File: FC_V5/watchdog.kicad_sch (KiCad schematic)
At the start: 40 parts, among them J10 Breakout, J11 Breakout, U1 TLV1704

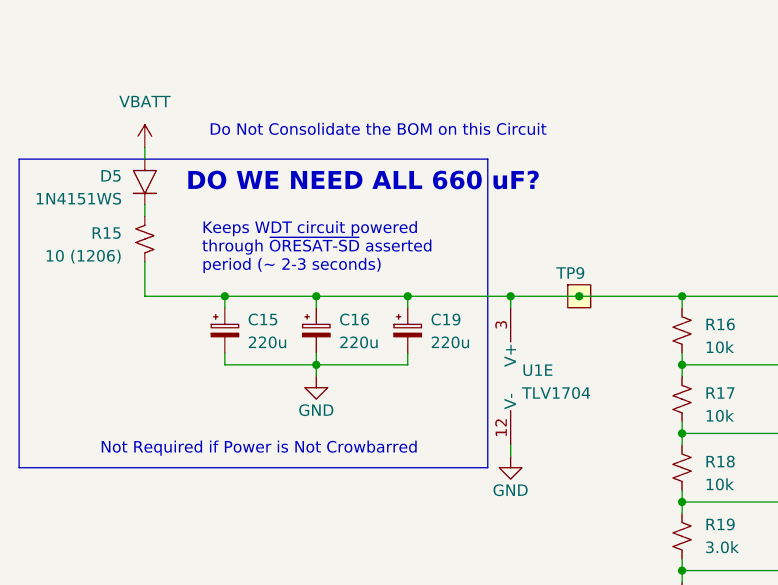
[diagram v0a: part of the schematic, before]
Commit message: Removed Unneed WDT Caps
We didn't need those caps because they are only required for OreSat.

NOTE: ALL OF THE SCHEMATIC REFERENCES ARE BUSTED AHHHHH
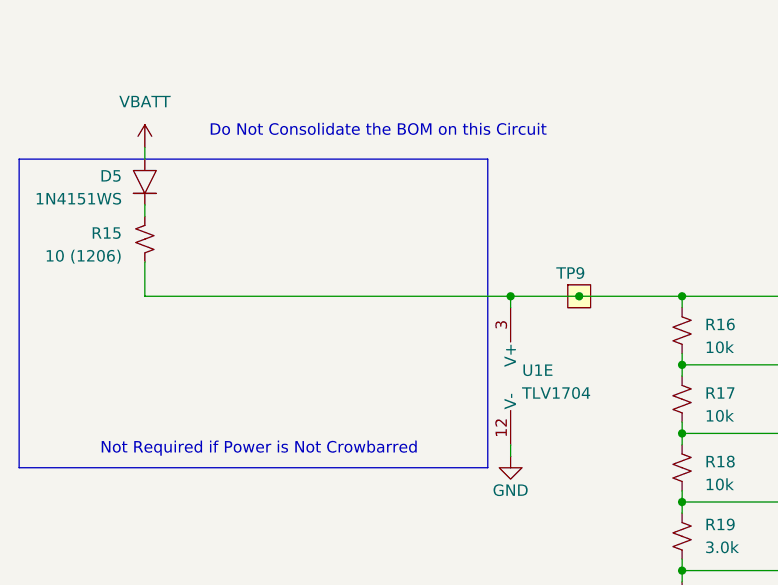
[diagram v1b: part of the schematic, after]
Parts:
- removed C15, C16, C19: 220u, Capacitor_Tantalum_SMD:CP_EIA-7361-38_AVX-V, symbol Device:C_Polarized_Small
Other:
- note removed: "DO WE NEED ALL 660 uF?"
- note removed: "Keeps WDT circuit powered through ~{ORESAT-SD} asserted period (~ 2-3 seconds)"

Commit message: More Stuff!
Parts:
- removed J10: Breakout, Connector_PinHeader_2.54mm:PinHeader_1x04_P2.54mm_Vertical, symbol Connector_Generic:Conn_01x04
- removed J11: Breakout, FC_DEV_BOARD:JST_BM04B-SRSS-TB(LF)(SN), symbol Connector_Generic:Conn_01x04
- removed JP2: SolderJumper_2_Open, Jumper:SolderJumper-2_P1.3mm_Open_RoundedPad1.0x1.5mm, symbol Jumper:SolderJumper_2_Open
- added C26, C28: 100nf, Capacitor_SMD:C_0402_1005Metric, symbol Adafruit ItsyBitsy RP2040-eagle-import:CAP_CERAMIC_0402NO
- added R23: 47k, Resistor_SMD:R_0603_1608Metric, symbol Device:R_Small_US
- added U3: AP22652, SOT26:SOT26, symbol Power_Management:AP22652
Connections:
- net GND: now also C26.2, C28.2, U3.2 (GND)
- net VBATT renamed WDT_BIAS
- net WDT_BIAS: now also C28.1, U3.6 (Output)
- new net: R23.2, U3.5 (ILIM)
- new net +3V3: C26.1, R23.1, U3.1 (Input)
- new net WDT_ENABLE: U3.3 (EN)
- no-connect marks 0 -> 1
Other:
- note removed: "Backup 5V Bias"

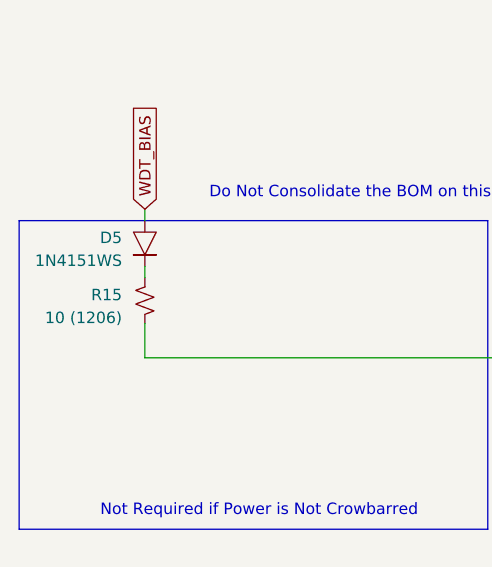
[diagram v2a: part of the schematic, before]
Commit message: Refactored Layout
The additional radio is on the top of the board now!
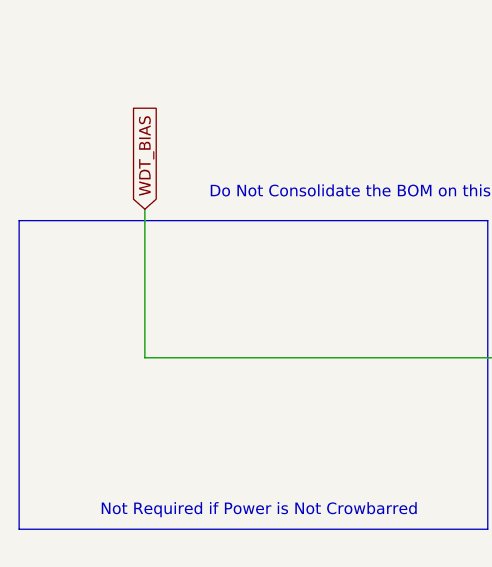
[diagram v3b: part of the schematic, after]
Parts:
- removed D5: 1N4151WS, Diode_SMD:D_SOD-323, symbol oresat-diodes:1N4151WS-HE3
- removed R15: 10 (1206), Resistor_SMD:R_1206_3216Metric, symbol Device:R_Small_US
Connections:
- net WDT-VIN is gone; now on net WDT_BIAS: R16.1, R30.1, R36.2, TP9.1, U1.3 (V+)
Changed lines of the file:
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@@
 	(wire
 		(pts
+			(xy 29.21 44.45) (xy 29.21 60.96)
+		)
+		(stroke
+			(width 0)
+			(type default)
+		)
+	)
+	(wire
+		(pts
 			(xy 88.9 68.58) (xy 185.42 68.58)
 		)
@@
 	(wire
 		(pts
-			(xy 29.21 57.15) (xy 29.21 60.96)
-		)
-		(stroke
-			(width 0)
-			(type default)
-		)
-	)
-	(wire
-		(pts
 			(xy 77.47 60.96) (xy 88.9 60.96)
 		)
@@
 	(wire
 		(pts
-			(xy 29.21 44.45) (xy 29.21 45.72)
-		)
-		(stroke
-			(width 0)
-			(type default)
-		)
-	)
-	(wire
-		(pts
 			(xy 201.93 142.24) (xy 204.47 142.24)
 		)
@@
 	(wire
 		(pts
-			(xy 29.21 50.8) (xy 29.21 52.07)
-		)
-		(stroke
-			(width 0)
-			(type default)
-		)
-	)
-	(wire
-		(pts
 			(xy 125.73 35.56) (xy 129.54 35.56)
 		)
@@
 	)
 	(symbol
-		(lib_id "oresat-diodes:1N4151WS-HE3")
-		(at 29.21 48.26 90)
-		(mirror x)
-		(unit 1)
-		(exclude_from_sim no)
-		(in_bom yes)
-		(on_board yes)
-		(dnp no)
-		(property "Reference" "D5"
-			(at 26.67 47.625 90)
-			(effects
-				(font
-					(size 1.27 1.27)
-				)
-				(justify left)
-			)
-		)
-		(property "Value" "1N4151WS"
-			(at 26.67 50.165 90)
-			(effects
-				(font
-					(size 1.27 1.27)
-				)
-				(justify left)
-			)
-		)
-		(property "Footprint" "Diode_SMD:D_SOD-323"
-			(at 34.29 48.26 0)
-			(effects
-				(font
-					(size 1.27 1.27)
-				)
-				(hide yes)
-			)
-		)
-		(property "Datasheet" "https://www.vishay.com/docs/85847/1n4151ws.pdf"
-			(at 36.83 48.26 0)
-			(effects
-				(font
-					(size 1.27 1.27)
-				)
-				(hide yes)
-			)
-		)
-		(property "Description" "Diode Standard 50V 150mA Surface Mount SOD-323"
-			(at 29.21 48.26 0)
-			(effects
-				(font
-					(size 1.27 1.27)
-				)
-				(hide yes)
-			)
-		)
-		(property "DPN" "112-1N4151WS-E3-08CT-ND"
-			(at 29.21 48.26 0)
-			(effects
-				(font
-					(size 1.27 1.27)
-				)
-				(hide yes)
-			)
-		)
-		(property "DST" "Digi-Key"
-			(at 29.21 48.26 0)
-			(effects
-				(font
-					(size 1.27 1.27)
-				)
-				(hide yes)
-			)
-		)
-		(property "MFR" "Vishay"
-			(at 29.21 48.26 0)
-			(effects
-				(font
-					(size 1.27 1.27)
-				)
-				(hide yes)
-			)
-		)
-		(property "MPN" "1N4151WS-E3-08"
-			(at 29.21 48.26 0)
-			(effects
-				(font
-					(size 1.27 1.27)
-				)
-				(hide yes)
-			)
-		)
-		(pin "1"
-		)
-		(pin "2"
-		)
-		(instances
-			(project "FC_V5"
-				(path "/c64c0d72-a9f6-4f3a-891e-1f647558f538/d3e26510-981a-4dd5-9b7d-a587e6324dc6"
-					(reference "D5")
-					(unit 1)
-				)
-			)
-		)
-	)
-	(symbol
 		(lib_id "Device:C_Small")
 		(at 170.18 128.27 0)
@@
 					(unit 1)
 				)
-			)
-		)
-	)
-	(symbol
-		(lib_id "Device:R_Small_US")
-		(at 29.21 54.61 0)
-		(mirror y)
-		(unit 1)
-		(exclude_from_sim no)
-		(in_bom yes)
-		(on_board yes)
-		(dnp no)
-		(property "Reference" "R15"
-			(at 26.67 53.975 0)
-			(effects
-				(font
-					(size 1.27 1.27)
-				)
-				(justify left)
-			)
-		)
-		(property "Value" "10 (1206)"
-			(at 26.67 56.515 0)
-			(effects
-				(font
-					(size 1.27 1.27)
-				)
-				(justify left)
-			)
-		)
-		(property "Footprint" "Resistor_SMD:R_1206_3216Metric"
-			(at 29.21 54.61 0)
-			(effects
-				(font
-					(size 1.27 1.27)
-				)
-				(hide yes)
-			)
-		)
-		(property "Datasheet" "~"
-			(at 29.21 54.61 0)
-			(effects
-				(font
-					(size 1.27 1.27)
-				)
-				(hide yes)
-			)
-		)
-		(property "Description" "10 Ohms ±1% 0.5W, 1/2W Chip Resistor 1206 (3216 Metric) Automotive AEC-Q200, Pulse Withstanding Thick Film"
-			(at 29.21 54.61 0)
-			(effects
-				(font
-					(size 1.27 1.27)
-				)
-				(hide yes)
-			)
-		)
-		(property "DPN" "RHM10.0AFCT-ND"
-			(at 29.21 54.61 0)
-			(effects
-				(font
-					(size 1.27 1.27)
-				)
-				(hide yes)
-			)
-		)
-		(property "DST" "Digi-Key"
-			(at 29.21 54.61 0)
-			(effects
-				(font
-					(size 1.27 1.27)
-				)
-				(hide yes)
-			)
-		)
-		(property "MFR" "Rohm Semiconductor"
-			(at 29.21 54.61 0)
-			(effects
-				(font
-					(size 1.27 1.27)
-				)
-				(hide yes)
-			)
-		)
-		(property "MPN" "ESR18EZPF10R0"
-			(at 29.21 54.61 0)
-			(effects
-				(font
-					(size 1.27 1.27)
-				)
-				(hide yes)
-			)
-		)
-		(pin "1"
-		)
-		(pin "2"
-		)
-		(instances
-			(project "FC_V5"
-				(path "/c64c0d72-a9f6-4f3a-891e-1f647558f538/d3e26510-981a-4dd5-9b7d-a587e6324dc6"
-					(reference "R15")
-					(unit 1)
-				)

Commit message: Almost Done with Layout!
Just been the VReg reset circuit and the V_RF Regulator and we are ready to rock and roll
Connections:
- net +3V3: now also R37.2
- net WDT_BIAS: no longer R37.2
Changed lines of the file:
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@@
 	(global_label "WDT_BIAS"
 		(shape input)
-		(at 238.76 64.77 90)
-		(fields_autoplaced yes)
-		(effects
-			(font
-				(size 1.27 1.27)
-			)
-			(justify left)
-		)
-		(property "Intersheetrefs" "${INTERSHEET_REFS}"
-			(at 238.76 52.9553 90)
-			(effects
-				(font
-					(size 1.27 1.27)
-				)
-				(justify left)
-				(hide yes)
-			)
-		)
-	)
-	(global_label "WDT_BIAS"
-		(shape input)
 		(at 29.21 44.45 90)
 		(fields_autoplaced yes)
@@
 					(unit 1)
 				)
+			)
+		)
+	)
+	(symbol
+		(lib_id "power:+3V3")
+		(at 238.76 64.77 0)
+		(unit 1)
+		(exclude_from_sim no)
+		(in_bom yes)
+		(on_board yes)
+		(dnp no)
+		(property "Reference" "#PWR0100"
+			(at 238.76 68.58 0)
+			(effects
+				(font
+					(size 1.27 1.27)
+				)
+				(hide yes)
+			)
+		)
+		(property "Value" "+3V3"
+			(at 234.696 63.5 0)
+			(effects
+				(font
+					(size 1.27 1.27)
+				)
+			)
+		)
+		(property "Footprint" ""
+			(at 238.76 64.77 0)
+			(effects
+				(font
+					(size 1.27 1.27)
+				)
+				(hide yes)
+			)
+		)
+		(property "Datasheet" ""
+			(at 238.76 64.77 0)
+			(effects
+				(font
+					(size 1.27 1.27)
+				)
+				(hide yes)
+			)
+		)
+		(property "Description" "Power symbol creates a global label with name \"+3V3\""
+			(at 238.76 64.77 0)
+			(effects
+				(font
+					(size 1.27 1.27)
+				)
+				(hide yes)
+			)
+		)
+		(pin "1"
+		)
+		(instances
+			(project "FC_V5"
+				(path "/c64c0d72-a9f6-4f3a-891e-1f647558f538/d3e26510-981a-4dd5-9b7d-a587e6324dc6"
+					(reference "#PWR0100")
+					(unit 1)
+				)

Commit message: Added a bunch of components
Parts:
- C20, C21, C22, C23, C24: value 10u -> 10uF
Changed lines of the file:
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@@
 			)
 		)
-		(property "Value" "10u"
+		(property "Value" "10uF"
 			(at 99.0663 121.92 90)
 			(effects
@@
 			)
 		)
-		(property "Value" "10u"
+		(property "Value" "10uF"
 			(at 177.8 130.1686 0)
 			(effects
@@
 			)
 		)
-		(property "Value" "10u"
+		(property "Value" "10uF"
 			(at 167.64 130.1686 0)
 			(effects
@@
 			)
 		)
-		(property "Value" "10u"
+		(property "Value" "10uF"
 			(at 133.35 127.6286 0)
 			(effects
@@
 			)
 		)
-		(property "Value" "10u"
+		(property "Value" "10uF"
 			(at 219.71 99.6886 0)
 			(effects
